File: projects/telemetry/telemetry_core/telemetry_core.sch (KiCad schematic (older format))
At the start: 42 parts, among them J1 MM_F_RA_20, J2 CONN_02X03, U1 ATMEGA16M1, U2 TPS560430YF, U3 MCP2561-E_SN, Y1 Crystal_SMD

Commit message: feat: set up schematic for rtc and add crystal
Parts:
- added C10, C11, C8, C9: C_0.1uF, footprints:C_0805_OEM, symbol formula:C_0.1uF
- added J2: SM06B-GHS-TB(LF)(SN), footprints:JST_SM06B-GHS-TB(LF)(SN), symbol formula:SM06B-GHS-TB(LF)(SN)
- added R2, R4: R_499, footprints:R_0805_OEM, symbol formula:R_499
- added U3: TXB0104PW, Package_SO:TSSOP-14_4.4x5mm_P0.65mm, symbol Logic_LevelTranslator:TXB0104PW
- added U4: LM3480-3.3, Package_TO_SOT_SMD:SOT-23, symbol Regulator_Linear:LM3480-3.3
- added U?: MCP79511-I_MS, footprints:MCP79511-I&slashMS, symbol formula:MCP79511-I_MS
- added Y?: Crystal_32_768kHz, footprints:Crystal_32_768kHZ, symbol formula:Crystal_32_768kHz
- renumbered J2 to J3, R8 to R10, R9 to R11, R10 to R12, R11 to R13, R2 to R3, R3 to R5, R4 to R6, R5 to R7, R6 to R8, R7 to R9
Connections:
- net labels added: +3V3, CS, CTS, RTS, RXD, TXD
- net labels removed: +3.3V
- wire segments 105 -> 135
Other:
- note added: "(recalculate resistances later)"
- note added: "32.768 kHz CRYSTAL\n"
- note added: "4-BIT 5V-3V3 LEVEL SHIFTER"
- note added: "CTS"
- note added: "JST GH 6-PIN CONNECTOR"
- note added: "LINEAR VOLTAGE REGULATOR"
- note added: "Pinout to RXD and TXD for Radio\n"
- note added: "REAL-TIME CLOCK"
- note added: "RTS"
- note added: "RX"
- note added: "TX"
- moved on the sheet: C1, C2, C5, C7, D4, D5, D6, R1, R10, R11, R7, R9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

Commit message: fix: update schematic symbol ref for JST connector
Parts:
- removed J2: SM06B-GHS-TB(LF)(SN), footprints:JST_SM06B-GHS-TB(LF)(SN), symbol formula:SM06B-GHS-TB(LF)(SN)
- added J?: JST_SM06B-GHS-TB_LF__SN_, footprints:JST_SM06B-GHS-TB_LF__SN_, symbol formula:JST_SM06B-GHS-TB_LF__SN_
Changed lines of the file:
@@
 Wire Notes Line
 	5400 750  5400 5750
-$Comp
-L formula:SM06B-GHS-TB(LF)(SN) J2
-U 1 1 618AE836
-P 14650 5050
-F 0 "J2" H 14543 4383 50  0000 C CNN
-F 1 "SM06B-GHS-TB(LF)(SN)" H 14543 4474 50  0000 C CNN
-F 2 "footprints:JST_SM06B-GHS-TB(LF)(SN)" H 14900 4850 50  0001 L BNN
-F 3 "https://www.jst-mfg.com/product/pdf/eng/eGH.pdf" H 14650 5050 50  0001 L BNN
-F 4 "JST" H 14900 4950 50  0001 L BNN "MANUFACTURER"
-F 5 "4.25mm" H 14900 4650 50  0001 L BNN "MAXIMUM_PACKAGE_HEIGHT"
-F 6 "Manufacturer Recommendations" H 14900 4750 50  0001 L BNN "STANDARD"
-F 7 "N/A" H 15250 4650 50  0001 L BNN "PARTREV"
-	1    14650 5050
-	-1   0    0    1
-$EndComp
 Text Notes 14000 4300 0    89   ~ 0
 JST GH 6-PIN CONNECTOR
@@
 Wire Notes Line
 	5650 2750 8900 2750
+$Comp
+L formula:JST_SM06B-GHS-TB_LF__SN_ J?
+U 1 1 61941897
+P 14650 5050
+F 0 "J?" H 14543 4383 50  0000 C CNN
+F 1 "JST_SM06B-GHS-TB_LF__SN_" H 14543 4474 50  0000 C CNN
+F 2 "footprints:JST_SM06B-GHS-TB_LF__SN_" H 14900 4850 50  0001 L BNN
+F 3 "https://www.jst-mfg.com/product/pdf/eng/eGH.pdf" H 14650 5050 50  0001 L BNN
+F 4 "JST" H 14900 4950 50  0001 L BNN "MANUFACTURER"
+F 5 "4.25mm" H 14900 4650 50  0001 L BNN "MAXIMUM_PACKAGE_HEIGHT"
+F 6 "Manufacturer Recommendations" H 14900 4750 50  0001 L BNN "STANDARD"
+F 7 "N/A" H 15250 4650 50  0001 L BNN "PARTREV"
+	1    14650 5050
+	-1   0    0    1
+$EndComp
 $EndSCHEMATC

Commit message: feat: connect rxd and txd for radio, big capacitor
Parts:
- removed R2, R4: R_499, footprints:R_0805_OEM, symbol formula:R_499
- added C?: C, symbol Device:C
- added R? (x3): R_499, footprints:R_0805_OEM, symbol formula:R_499
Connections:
- net SCK is gone; now on net RXD_RADIO: J3.3 (P3), U1.12 ((PCINT20/ADC1/RXD/RXLIN/ICP1A/SCK_A)PD4)
- net TXD is gone; now on net MOSI: J?.3
- net +3V3: now also U?.9 (MFP)
- net 12V: now also C?.1; no longer J1.2
- net CS: now also U3.10 (B4)
- net GND: now also U?.3 (VBAT), U?.5 (VSS)
- net MISO: now also R?.2
- net MOSI: now also R?.2
- net SCK_ATMEGA: now reaches U3.11 (B3)
- net SCK_ATMEGA: now also R?.1
- net SO_ATMEGA: now reaches U3.12 (B2)
- net SO_ATMEGA: now also R?.1
- net SI_ATMEGA: now reaches U3.13 (B1)
- net SI_ATMEGA: now also R?.1
- net SI_RTC: now reaches U3.2 (A1)
- net SI_RTC: now also U?.6 (SI)
- net SO_RTC: now reaches U3.3 (A2)
- net SO_RTC: now also U?.7 (SO)
- net SCK_RTC: now reaches U3.4 (A3)
- net SCK_RTC: now also U?.8 (SCK)
- net CS_RTC: now reaches U3.5 (A4)
- net CS_RTC: now also U?.4 (*CS)
- net CTS renamed CTS_RADIO
- net RTS renamed RTS_RADIO
- net RXD renamed RXD_RADIO
- net RXD_RADIO: now also R?.2
- new net 12V_IN: C?.2, J1.2
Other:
- note added: "CAPACITOR HERE, DIODES BEHIND CAPACITOR.\ncheck notes\n"
- note added: "Check if needs pullup resistor"
- note added: "Clarify radio connections"
- note added: "Generic capacitor to \ndetermine after assembly\n"
- note added: "Resistors for RTC and Radio connections for MOSI and SCK pins\n"
- note added: "swapped"
- note removed: "(recalculate resistances later)"
- note removed: "Pinout to RXD and TXD for Radio\n"
- moved on the sheet: C10, C11, C8, C9, U3, U4, U?, Y?

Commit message: feat: spec out caps for rtc, ATMEGA connects
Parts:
- removed R? (x3): R_499, footprints:R_0805_OEM, symbol formula:R_499
- added C10, C9: C, symbol Device:C
- added C12: C_10nF, footprints:C_1206_OEM, symbol formula:C_10nF
- added R11: R_475, footprints:R_0805_OEM, symbol formula:R_475
- gave numbers to parts that had none: 4
- renumbered C9 to C11, C10 to C13, C11 to C14, C8 to C16, R12 to R10, R13 to R12, R3 to R2, R5 to R3, R6 to R4, R7 to R5, R8 to R6, R9 to R7, R10 to R8, R11 to R9, U3 to U4, U4 to U5, U3 to U6
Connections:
- net +3V3: now also C12.1, R11.1; no longer U3.10 (VCC), U3.9 (MFP)
- net CTS_RADIO: now also U1.26 ((PCINT5/ADC6/INT2/ACMPN1/AMP2-)PB5); no longer U1.28 ((PCINT7/ADC4/SCK/PSCOUT0B)PB7)
- net GND: now also C10.1, C9.1
- net P_LED_1: now also U1.16 ((PCINT2/ADC5/INT1/ACMPN0)PB2); no longer U1.8 ((PCINT0/MISO/PSCOUT2A)PB0)
- net P_LED_2: now also U1.24 ((PCINT4/AMP0+)PB4); no longer U1.23 ((PCINT3/AMP0-)PB3)
- net P_LED_3: now also U1.23 ((PCINT3/AMP0-)PB3); no longer U1.9 ((PCINT1/MOSI/PSCOUT2B)PB1)
- net SI_ATMEGA: now also U1.9 ((PCINT1/MOSI/PSCOUT2B)PB1)
- net SO_ATMEGA: now also U1.8 ((PCINT0/MISO/PSCOUT2A)PB0)
- net at U3.1 (X1), Y2.1: now also C9.2
- net at U3.2 (X2), Y2.2: now also C10.2
- net CS renamed CSB
- net CS_RTC renamed CSB_RTC
- new net: C12.2, U3.10 (VCC)
- new net: R11.2, U3.9 (MFP)
- no-connect marks 15 -> 13
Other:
- note added: "Check if needs\npullup resistor"
- note added: "See notes for capacitors."
- note added: "The real-time clock to be used by the \nATMEGA when dealing with incoming data."
- note added: "for RTC"
- note added: "for radio"
- note removed: "Check if needs pullup resistor"
- note removed: "Resistors for RTC and Radio connections for MOSI and SCK pins\n"
- moved on the sheet: C11, C13, C14, C8, U3, U4, U5, Y2

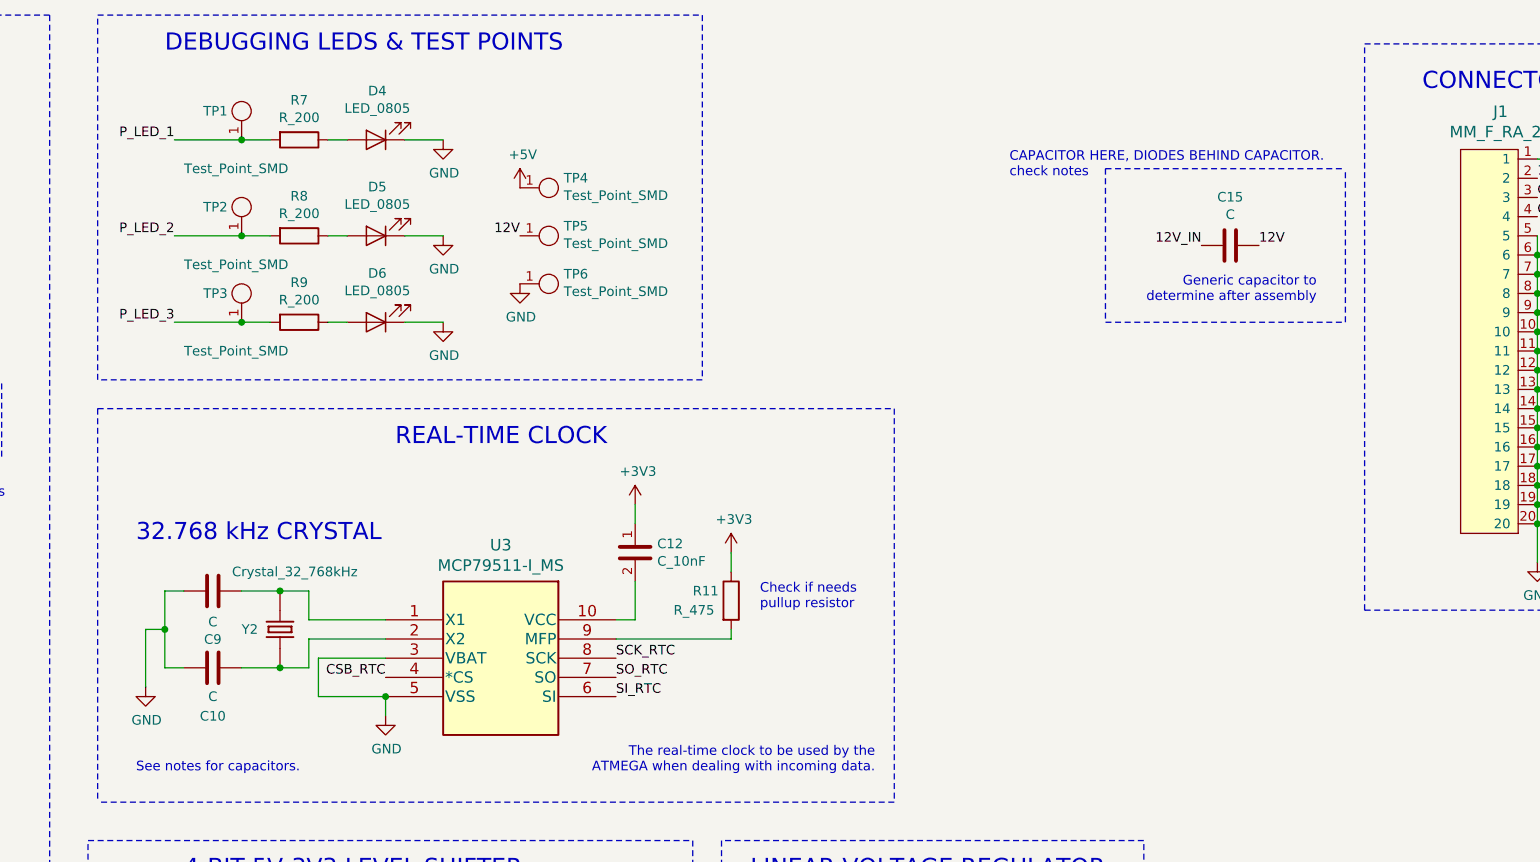
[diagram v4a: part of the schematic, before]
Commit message: add 10pf and tht cap, update schematic
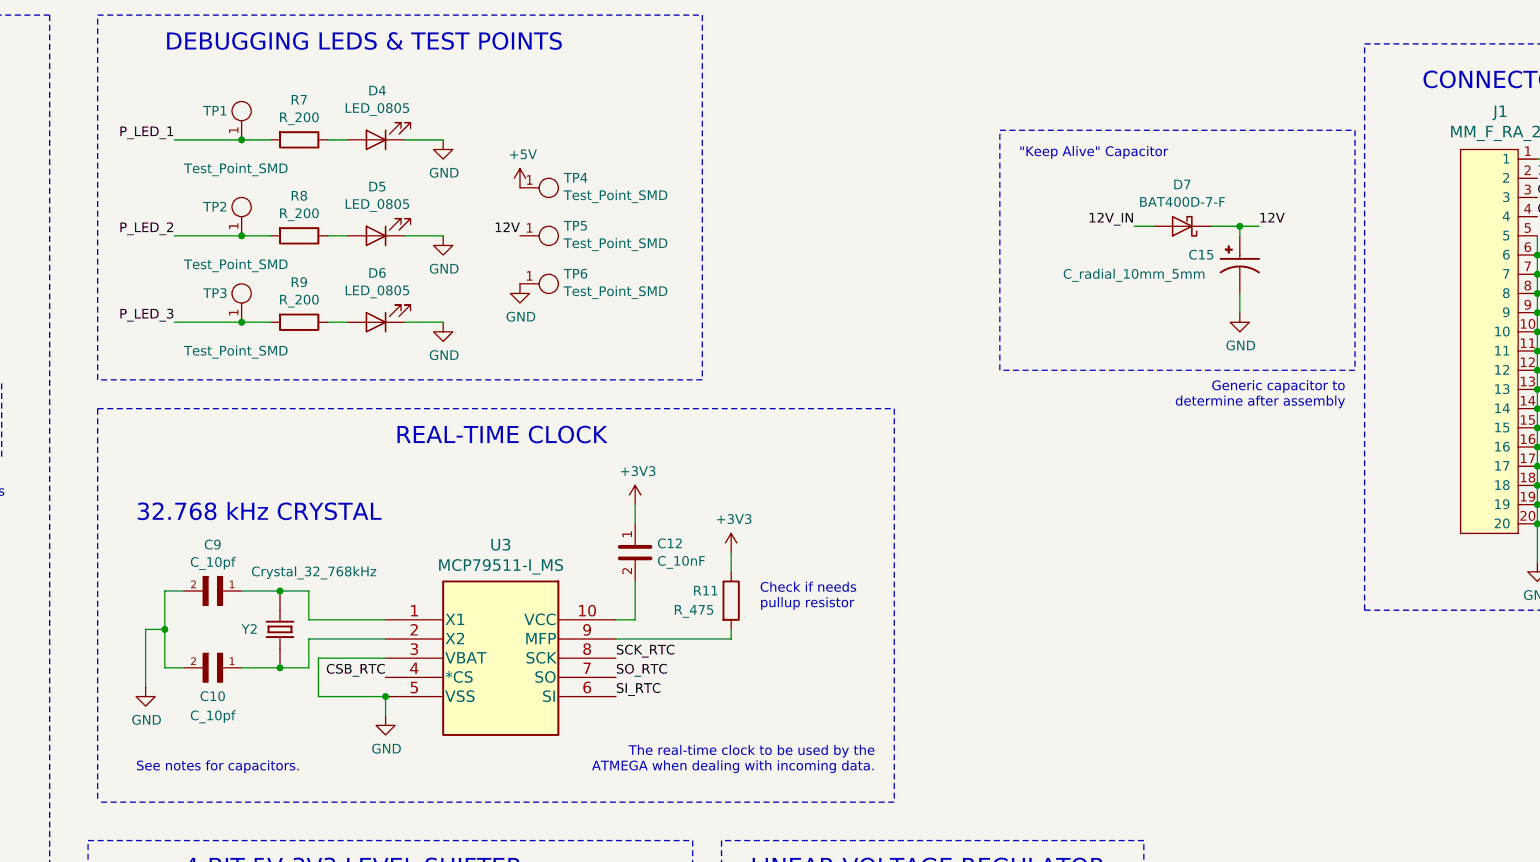
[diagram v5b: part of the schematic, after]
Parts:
- removed C10, C15, C9: C, symbol Device:C
- added C10, C9: C_10pf, footprints:C_10pf, symbol formula:C_10pf
- added C15: C_radial_10mm_5mm, footprints:C_radial_10mm_5mm, symbol formula:C_radial_10mm_5mm
- added D7: BAT400D-7-F, footprints:SOT-23-3_OEM, symbol formula:BAT400D-7-F
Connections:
- net 12V: now also C15.P, D7.1 (K)
- net 12V_IN: now also D7.2 (A)
- net GND: now also C10.2, C15.N, C9.2
- net at U3.1 (X1), Y2.1: now also C9.1
- net at U3.2 (X2), Y2.2: now also C10.1
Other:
- note added: ""Keep Alive" Capacitor"
- note removed: "CAPACITOR HERE, DIODES BEHIND CAPACITOR.\ncheck notes\n"
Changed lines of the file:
@@
 Wire Wire Line
 	6750 4150 6600 4150
-Text Notes 5850 3500 0    89   ~ 0
-32.768 kHz CRYSTAL\n
 $Comp
 L formula:JST_SM06B-GHS-TB_LF__SN_ J2
@@
 Text Label 6750 6150 2    50   ~ 0
 SI_RTC
-Text Notes 10400 1600 0    50   ~ 0
-CAPACITOR HERE, DIODES BEHIND CAPACITOR.\ncheck notes\n
+Text Notes 10450 1500 0    50   ~ 0
+"Keep Alive" Capacitor
 Text Label 7550 6150 0    50   ~ 0
 SI_ATMEGA
@@
 Text Label 3900 1800 0    50   ~ 0
 CTS_RADIO
-Text Notes 12000 2250 2    50   ~ 0
+Text Notes 12150 2800 2    50   ~ 0
 Generic capacitor to \ndetermine after assembly\n
 Text Notes 4750 2750 0    50   ~ 0
 swapped
-Text Label 13150 1600 0    50   ~ 0
-12V_IN
-Text Label 11400 1950 2    50   ~ 0
-12V_IN
-Text Label 11700 1950 0    50   ~ 0
-12V
-$Comp
-L Device:C C15
-U 1 1 61D6EFCD
-P 11550 1950
-F 0 "C15" V 11298 1950 50  0000 C CNN
-F 1 "C" V 11389 1950 50  0000 C CNN
-F 2 "" H 11588 1800 50  0001 C CNN
-F 3 "~" H 11550 1950 50  0001 C CNN
-	1    11550 1950
-	0    1    1    0
-$EndComp
-Wire Notes Line
-	10900 1550 10900 2350
-Wire Notes Line
-	10900 2350 12150 2350
-Wire Notes Line
-	12150 2350 12150 1550
-Wire Notes Line
-	10900 1550 12150 1550
 Text Label 3900 1400 0    50   ~ 0
 SI_ATMEGA
@@
 	6800 4300 7150 4300
 $Comp
-L Device:C C10
-U 1 1 61EEE253
-P 6250 4150
-F 0 "C10" V 5998 4150 50  0000 C CNN
-F 1 "C" V 6100 4150 50  0000 C CNN
-F 2 "" H 6288 4000 50  0001 C CNN
-F 3 "~" H 6250 4150 50  0001 C CNN
-	1    6250 4150
-	0    -1   -1   0
-$EndComp
-$Comp
-L Device:C C9
-U 1 1 61F01F6F
-P 6250 3750
-F 0 "C9" V 5998 3750 50  0000 C CNN
-F 1 "C" V 6089 3750 50  0000 C CNN
-F 2 "" H 6288 3600 50  0001 C CNN
-F 3 "~" H 6250 3750 50  0001 C CNN
-	1    6250 3750
-	0    -1   -1   0
-$EndComp
-$Comp
 L power:GND #PWR?
 U 1 1 61F2BF60
@@
 P 6600 3950
 F 0 "Y2" V 6600 3750 50  0000 L CNN
-F 1 "Crystal_32_768kHz" V 6300 3700 50  0000 L CNN
+F 1 "Crystal_32_768kHz" V 6300 3800 50  0000 L CNN
 F 2 "footprints:Crystal_32_768kHZ" H 6300 4250 50  0001 L BNN
 F 3 "https://www.jauch.com/downloadfile/57fde22d50dbf_d3c203011c87952f2834/jtx310-auto-2-210512.pdf" H 6600 3950 50  0001 L BNN
@@
 Wire Notes Line
 	9800 2800 9800 4850
+Text Notes 5850 3400 0    89   ~ 0
+32.768 kHz CRYSTAL\n
+$Comp
+L formula:C_10pf C9
+U 1 1 620FD9D6
+P 6300 3750
+F 0 "C9" H 6350 3510 50  0000 C CNN
+F 1 "C_10pf" H 6350 3601 50  0000 C CNN
+F 2 "footprints:C_10pf" H 6300 3750 50  0001 L BNN
+F 3 "https://content.kemet.com/datasheets/F3102_MIL-PRF-55681.pdf" H 6300 3750 50  0001 L BNN
+F 4 "https://www.digikey.com/en/products/detail/kemet/CDR31BP100BJUS7185/3738523" H 5900 3550 50  0001 C CNN "PurchasingLink"
+	1    6300 3750
+	-1   0    0    1
+$EndComp
+$Comp
+L formula:C_10pf C10
+U 1 1 620F96C6
+P 6300 4150
+F 0 "C10" H 6350 4300 50  0000 C CNN
+F 1 "C_10pf" H 6350 4400 50  0000 C CNN
+F 2 "footprints:C_10pf" H 6300 4150 50  0001 L BNN
+F 3 "https://content.kemet.com/datasheets/F3102_MIL-PRF-55681.pdf" H 6300 4150 50  0001 L BNN
+F 4 "https://www.digikey.com/en/products/detail/kemet/CDR31BP100BJUS7185/3738523" H 5900 3950 50  0001 C CNN "PurchasingLink"
+	1    6300 4150
+	-1   0    0    1
+$EndComp
+$Comp
+L formula:C_radial_10mm_5mm C15
+U 1 1 6204B3A8
+P 11600 2000
+F 0 "C15" V 11600 1800 50  0000 C CNN
+F 1 "C_radial_10mm_5mm" V 11700 1450 50  0000 C CNN
+F 2 "footprints:C_radial_10mm_5mm" H 11600 2000 50  0001 L BNN
+F 3 "" H 11600 2000 50  0001 L BNN
+F 4 "0.6" H 11600 2000 50  0001 L BNN "b_nom"
+F 5 "PANASONIC" H 11600 2000 50  0001 L BNN "MF"
+F 6 "0.65" H 11600 2000 50  0001 L BNN "b_max"
+F 7 "10" H 11600 2000 50  0001 L BNN "D_nom"
+F 8 "20" H 11600 2000 50  0001 L BNN "A_max"
+F 9 "EB-A" H 11600 2000 50  0001 L BNN "DESCRIPTION"
+F 10 "5" H 11600 2000 50  0001 L BNN "e_nom"
+F 11 "28-FEB-20" H 11600 2000 50  0001 L BNN "PARTREV"
+	1    11600 2000
+	0    1    1    0
+$EndComp
+Text Label 11700 1850 0    50   ~ 0
+12V
+Text Label 13150 1600 0    50   ~ 0
+12V_IN
+Text Label 11050 1850 2    50   ~ 0
+12V_IN
+$Comp
+L power:GND #PWR?
+U 1 1 621C3D8D
+P 11600 2300
+F 0 "#PWR?" H 11600 2050 50  0001 C CNN
+F 1 "GND" H 11605 2127 50  0000 C CNN
+F 2 "" H 11600 2300 50  0001 C CNN
+F 3 "" H 11600 2300 50  0001 C CNN
+	1    11600 2300
+	1    0    0    -1
+$EndComp
+$Comp
+L formula:BAT400D-7-F D7
+U 1 1 621C7C27
+P 11300 1850
+F 0 "D7" H 11300 1634 50  0000 C CNN
+F 1 "BAT400D-7-F" H 11300 1725 50  0000 C CNN
+F 2 "footprints:SOT-23-3_OEM" H 11200 1850 50  0001 C CNN
+F 3 "https://www.diodes.com/assets/Datasheets/ds30182.pdf" H 11300 1950 50  0001 C CNN
+F 4 "https://www.digikey.com/products/en?keywords=BAT400D-FDICT-ND" H 11600 2250 60  0001 C CNN "PurchasingLink"
+	1    11300 1850
+	-1   0    0    1
+$EndComp
+Wire Wire Line
+	11450 1850 11600 1850
+Wire Wire Line
+	11600 1850 11600 1900
+Wire Wire Line
+	11600 2200 11600 2300
+Wire Wire Line
+	11600 1850 11700 1850
+Connection ~ 11600 1850
+Wire Wire Line
+	11150 1850 11050 1850
+Wire Notes Line
+	12200 1350 12200 2600
+Wire Notes Line
+	12200 2600 10350 2600
+Wire Notes Line
+	10350 2600 10350 1350
+Wire Notes Line
+	10350 1350 12200 1350
 $EndSCHEMATC

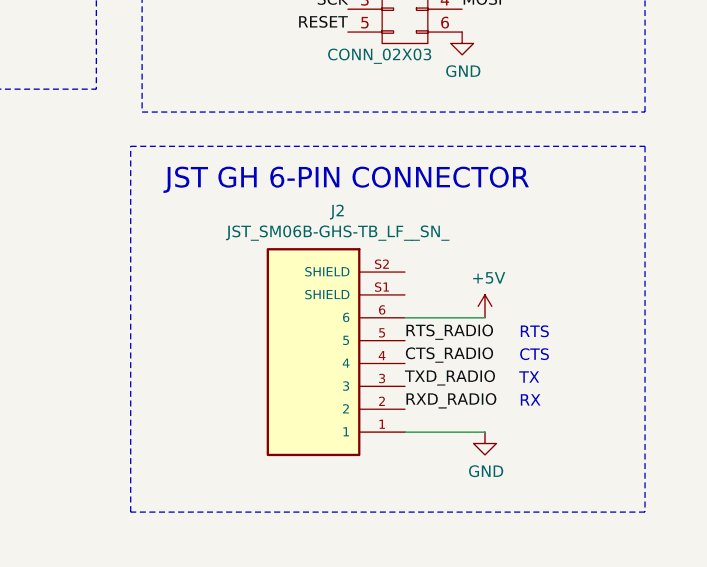
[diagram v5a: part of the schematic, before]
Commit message: fix MCP79511, start layout
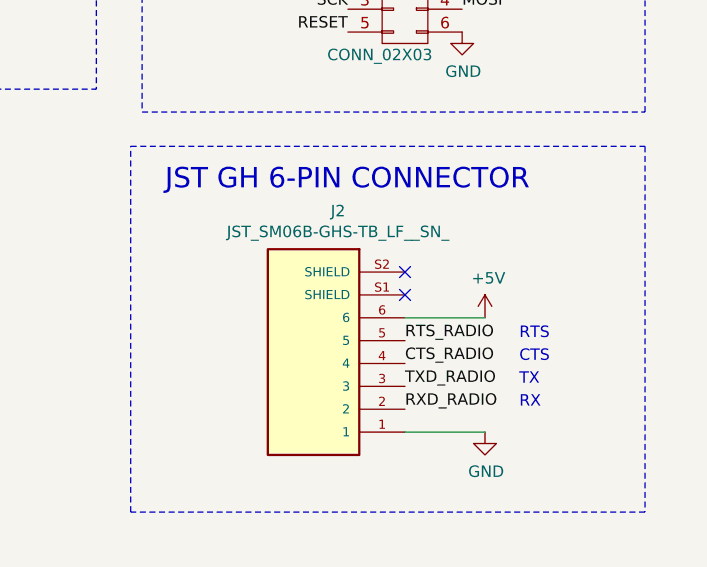
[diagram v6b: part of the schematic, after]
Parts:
- L1: footprint formula:L_100uH -> footprints:L_100uH_OEM
- U3: footprint footprints:MCP79511-I&slashMS -> footprints:MCP79511_I_MS
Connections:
- no-connect marks 13 -> 15
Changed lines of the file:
@@
 F 0 "L1" H 4550 8800 50  0000 C CNN
 F 1 "L_100uH" H 4550 8650 50  0000 C CNN
-F 2 "formula:L_100uH" H 4450 8500 50  0001 C CNN
+F 2 "footprints:L_100uH_OEM" H 4450 8500 50  0001 C CNN
 F 3 "https://product.tdk.com/info/en/catalog/datasheets/inductor_commercial_decoupling_nlfv32-ef_en.pdf" H 4450 8550 50  0001 C CNN
 F 4 "Digikey" H 4650 8500 50  0001 C CNN "MFN"
@@
 	1    0    0    -1
 $EndComp
-Connection ~ 7150 4300
-$Comp
-L formula:MCP79511-I_MS U3
-U 1 1 619A9C99
-P 6650 3900
-F 0 "U3" H 7750 4289 60  0000 C CNN
-F 1 "MCP79511-I_MS" H 7750 4183 60  0000 C CNN
-F 2 "footprints:MCP79511-I&slashMS" H 7750 4150 60  0001 C CNN
-F 3 "https://ww1.microchip.com/downloads/en/DeviceDoc/MCP7951X-MCP7952X-Battery-Backed-SPI-RTCC-20002300C.pdf" H 7150 3900 60  0001 C CNN
-F 4 "https://www.digikey.com/short/8h8hqbn4" H 7750 3250 50  0001 C CNN "PurchasingLink"
-	1    6650 3900
-	1    0    0    -1
-$EndComp
 $Comp
 L power:+3V3 #PWR?
@@
 Wire Notes Line
 	10350 1350 12200 1350
+NoConn ~ 15050 4650
+NoConn ~ 15050 4750
+$Comp
+L formula:MCP79511-I_MS U3
+U 1 1 6229D803
+P 6650 3900
+F 0 "U3" H 7750 4289 60  0000 C CNN
+F 1 "MCP79511-I_MS" H 7750 4183 60  0000 C CNN
+F 2 "footprints:MCP79511_I_MS" H 7750 4150 60  0001 C CNN
+F 3 "https://ww1.microchip.com/downloads/en/DeviceDoc/MCP7951X-MCP7952X-Battery-Backed-SPI-RTCC-20002300C.pdf" H 7150 3900 60  0001 C CNN
+F 4 "https://www.digikey.com/short/8h8hqbn4" H 7750 3250 50  0001 C CNN "PurchasingLink"
+	1    6650 3900
+	1    0    0    -1
+$EndComp
+Connection ~ 7150 4300
 $EndSCHEMATC

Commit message: feat: near-complete layout
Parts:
- renumbered L1 to L101
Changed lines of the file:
@@
 $EndComp
 $Comp
-L formula:L_100uH L1
+L formula:L_100uH L101
 U 1 1 5F881F17
 P 4550 8700
-F 0 "L1" H 4550 8800 50  0000 C CNN
+F 0 "L101" H 4550 8800 50  0000 C CNN
 F 1 "L_100uH" H 4550 8650 50  0000 C CNN
 F 2 "footprints:L_100uH_OEM" H 4450 8500 50  0001 C CNN

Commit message: feat: complete v1 layout
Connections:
- net P_LED_2: now also U1.23 ((PCINT3/AMP0-)PB3); no longer U1.24 ((PCINT4/AMP0+)PB4)
- net P_LED_3: now also U1.24 ((PCINT4/AMP0+)PB4); no longer U1.23 ((PCINT3/AMP0-)PB3)
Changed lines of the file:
@@
 P_LED_1
 Text Label 3900 1600 0    50   ~ 0
+P_LED_2
+Text Label 3900 1700 0    50   ~ 0
 P_LED_3
-Text Label 3900 1700 0    50   ~ 0
-P_LED_2
 $Comp
 L power:PWR_FLAG #FLG?
